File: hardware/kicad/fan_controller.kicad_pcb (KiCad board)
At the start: 2 copper layers, 75 x 60 mm, 84 parts, among them J1 12V IN, J10 AIN2, J11 AIN3, J12 AIN4, J13 AIN5, J14 AIN6, J2 BluePill A, J3 BluePill B, J4 USB int, J5 FAN1, J6 FAN2, J7 FAN3, J8 FAN4, J9 AIN1, Q1 BSS138, Q2 BSS138, Q3 BSS138, Q4 BSS138, U1 USBLC6-2SC6

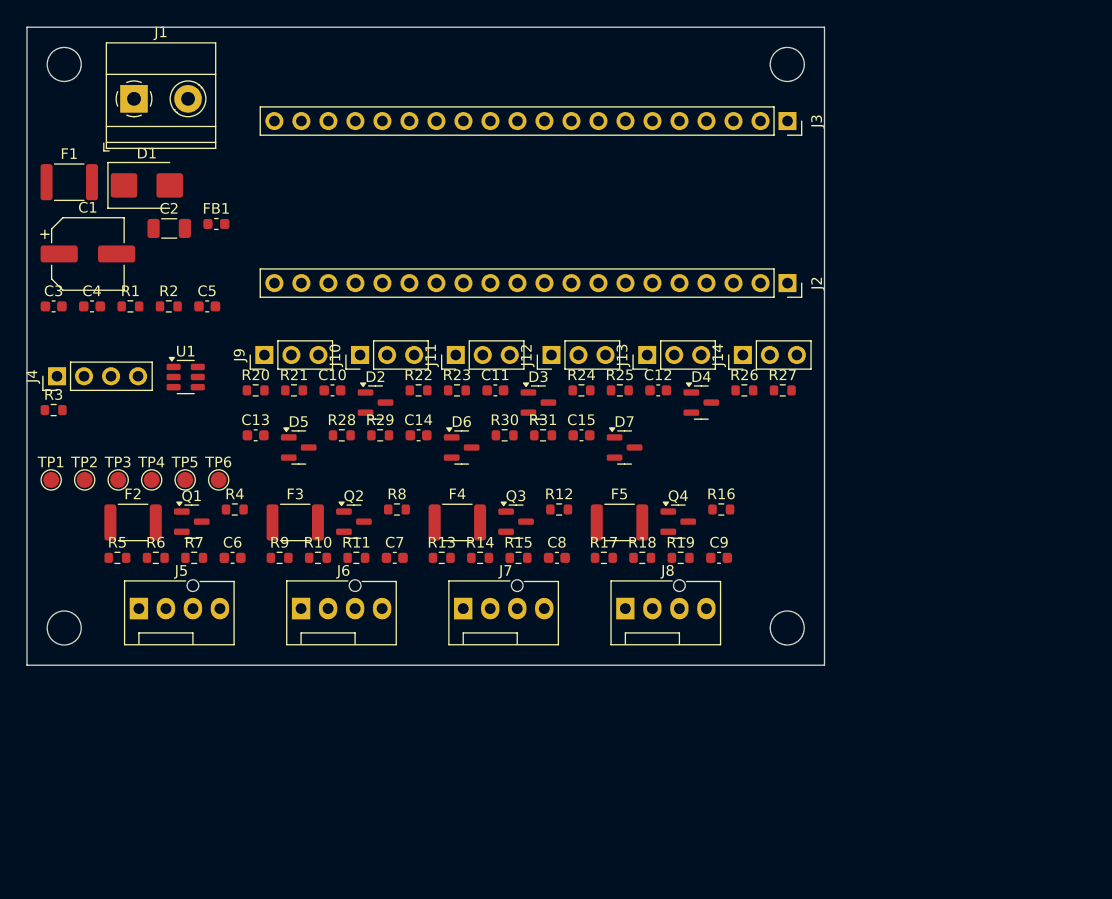
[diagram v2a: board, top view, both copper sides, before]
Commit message: hw: resave project in KiCad 10 file format
Signed-off-by: Roman Skakun <rm.skakun@gmail.com>
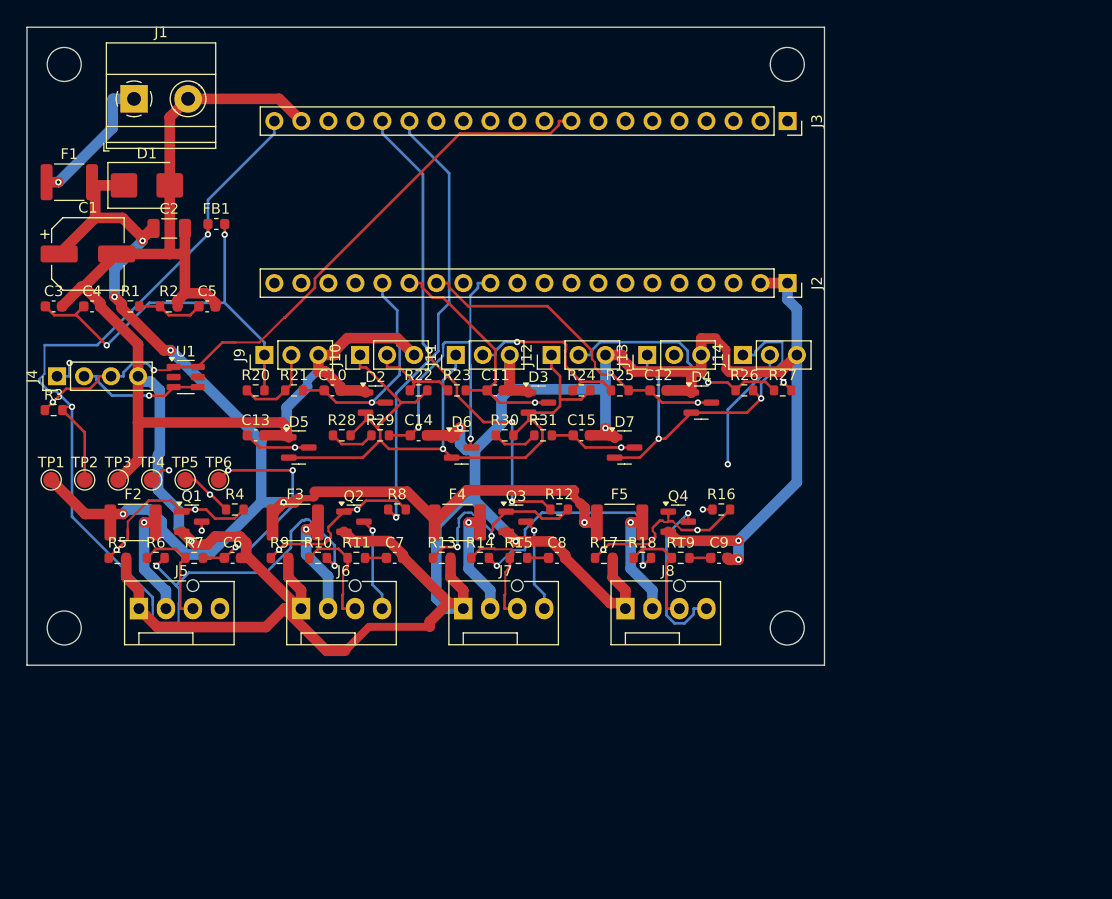
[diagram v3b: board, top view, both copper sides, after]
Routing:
- net GND: track 0.00 -> 370.6 mm, vias 0 -> 7
- net +3V3A: track 0.00 -> 144.6 mm, vias 0 -> 5
- net +3V3: track 0.00 -> 129.1 mm, vias 0 -> 6
- net +12V: track 0.00 -> 115.5 mm, vias 0 -> 6
- net USB_DP: track 0.00 -> 62.5 mm, vias 0 -> 2
- net FAN3_PWM: track 0.00 -> 46.3 mm, vias 0 -> 3
- net FAN2_PWM: track 0.00 -> 41.9 mm, vias 0 -> 1
- net AIN3: track 0.00 -> 31.5 mm, vias 0 -> 1
- net AIN5: track 0.00 -> 31.5 mm, vias 0 -> 2
- net AIN2: track 0.00 -> 23.3 mm, vias 0 -> 1
- net AIN4_IN: track 0.00 -> 22.3 mm, vias 0 -> 1
- net AIN1: track 0.00 -> 21.2 mm, vias 0 -> 1
- net FAN1_TACH: track 0.00 -> 21.1 mm, vias 0 -> 3
- net FAN3_PWM_G: track 0.00 -> 19.3 mm, vias 0 -> 2
- net AIN3_IN: track 0.00 -> 17.1 mm, vias 0 -> 1
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
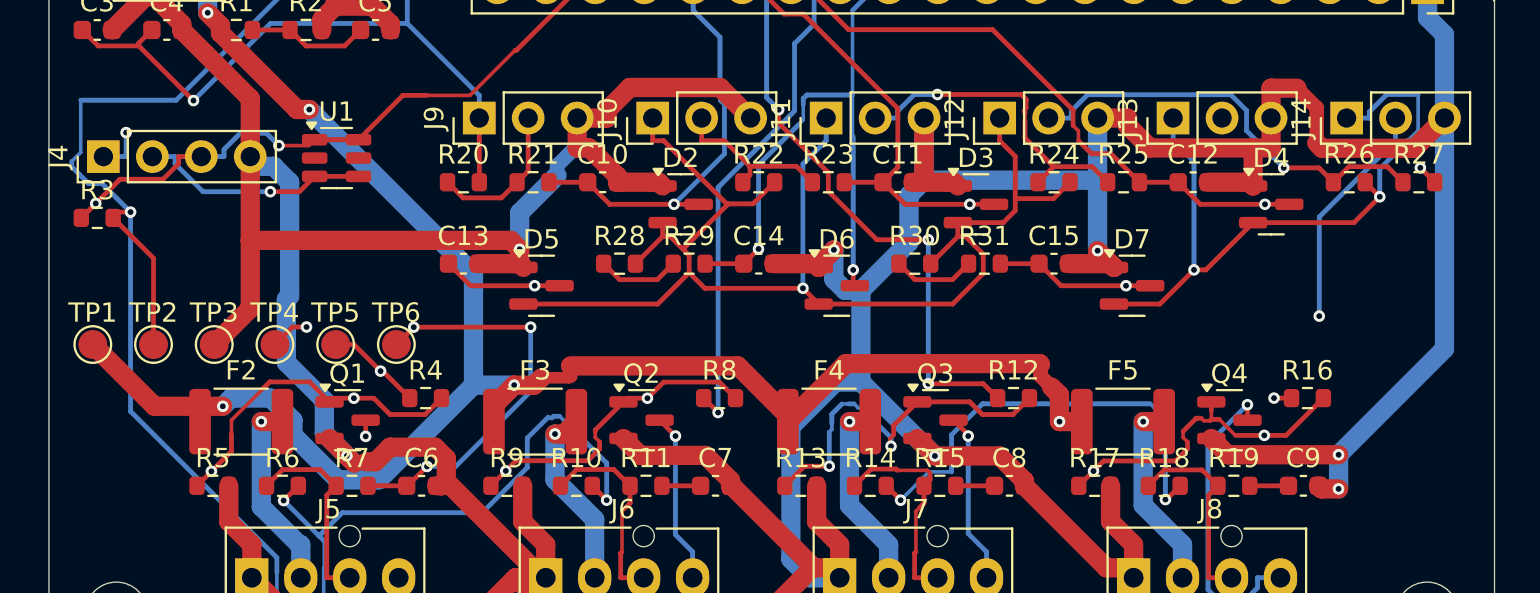
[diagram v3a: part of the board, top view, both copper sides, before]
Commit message: hw: remove dangling stub vias and traces from routing cleanup
20 vias left connected on only one copper layer, plus the short
track stubs feeding them, after an earlier routing edit. DRC now
reports 0 errors (was 0 before too) and 0 dangling-via/track
warnings; all affected nets remain fully connected.

Signed-off-by: Roman Skakun <rm.skakun@gmail.com>
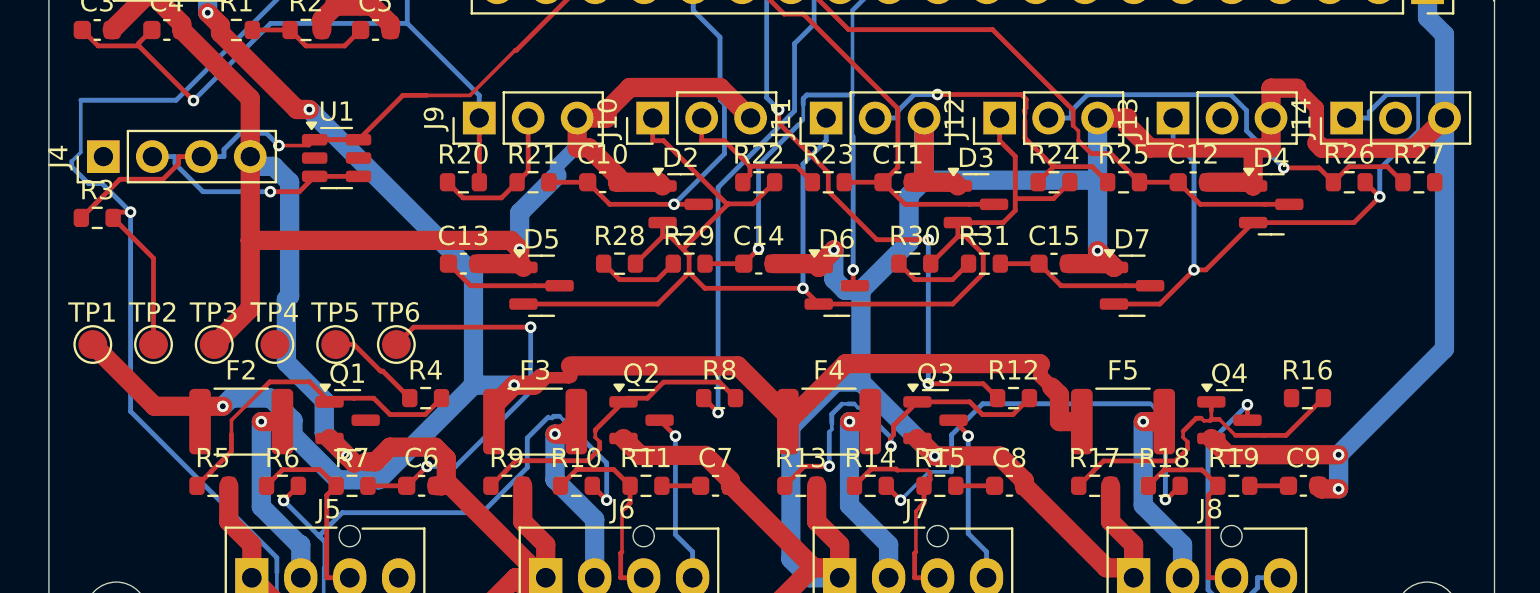
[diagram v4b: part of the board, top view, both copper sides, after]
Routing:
- net AIN6_IN: track 16.2 -> 4.30 mm, vias 1 -> 0
- net +5V: track 2.42 -> 0.00 mm, vias 1 -> 0
- net NRST: track 2.02 -> 0.00 mm, vias 1 -> 0
- net AIN4: track 7.29 -> 6.24 mm, vias 2 -> 0
- net FAN4_PWM: track 0.91 -> 0.00 mm, vias 1 -> 0
- net FAN1_PWM_OUT: track 0.84 -> 0.00 mm, vias 1 -> 0
- net USB_DP: vias 2 -> 1
- net FAN4_PWM_G: vias 2 -> 0
- net FAN2_PWM_G: vias 2 -> 0
- net FAN1_TACH: vias 3 -> 2
- net FAN1_PWM_G: vias 2 -> 0
- net FAN1_PWM: vias 1 -> 0
- net AIN6: vias 1 -> 0
- net AIN3: vias 1 -> 0
- net AIN2: vias 1 -> 0
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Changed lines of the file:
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@@
 		(net "FAN2_PWM_G")
 	)
-	(via
-		(at 23.7024 49.131)
-		(size 0.6)
-		(drill 0.3)
-		(layers "F.Cu" "B.Cu")
-		(net "FAN2_PWM_G")
-	)
-	(via
-		(at 31.0513 45.3609)
-		(size 0.6)
-		(drill 0.3)
-		(layers "F.Cu" "B.Cu")
-		(net "FAN2_PWM_G")
-	)
 	(segment
 		(start 33.865 30.825)
@@
 		(net "AIN2")
 	)
-	(via
-		(at 47.7772 35.3)
-		(size 0.6)
-		(drill 0.3)
-		(layers "F.Cu" "B.Cu")
-		(net "AIN2")
-	)
 	(segment
 		(start 64.31 49.905)
@@
 		(net "FAN1_PWM_G")
 	)
-	(via
-		(at 8.4289 49.1545)
-		(size 0.6)
-		(drill 0.3)
-		(layers "F.Cu" "B.Cu")
-		(net "FAN1_PWM_G")
-	)
-	(via
-		(at 15.8212 45.3609)
-		(size 0.6)
-		(drill 0.3)
-		(layers "F.Cu" "B.Cu")
-		(net "FAN1_PWM_G")
-	)
-	(segment
-		(start 71.9 34.155)
-		(end 71.1523 33.4073)
-		(width 0.25)
-		(layer "F.Cu")
-		(net "AIN4")
-	)
 	(segment
 		(start 21.875 39.525)
@@
 		(net "AIN4")
 	)
-	(via
-		(at 71.1523 33.4073)
-		(size 0.6)
-		(drill 0.3)
-		(layers "F.Cu" "B.Cu")
-		(net "AIN4")
-	)
-	(via
-		(at 25.2016 39.525)
-		(size 0.6)
-		(drill 0.3)
-		(layers "F.Cu" "B.Cu")
-		(net "AIN4")
-	)
-	(segment
-		(start 63.5596 45.355)
-		(end 64.47 45.355)
-		(width 0.25)
-		(layer "F.Cu")
-		(net "FAN4_PWM")
-	)
-	(via
-		(at 63.5596 45.355)
-		(size 0.6)
-		(drill 0.3)
-		(layers "F.Cu" "B.Cu")
-		(net "FAN4_PWM")
-	)
 	(segment
 		(start 61.5573 47.2894)
@@
 		(net "FAN4_PWM_G")
 	)
-	(via
-		(at 54.1955 49.1395)
-		(size 0.6)
-		(drill 0.3)
-		(layers "F.Cu" "B.Cu")
-		(net "FAN4_PWM_G")
-	)
-	(via
-		(at 63.0561 47.2894)
-		(size 0.6)
-		(drill 0.3)
-		(layers "F.Cu" "B.Cu")
-		(net "FAN4_PWM_G")
-	)
 	(segment
 		(start 36.05 38.38)
@@
 	)
 	(via
-		(at 52.4304 46.575)
-		(size 0.6)
-		(drill 0.3)
-		(layers "F.Cu" "B.Cu")
-		(net "+12V")
-	)
-	(via
 		(at 13.5105 30.3818)
 		(size 0.6)
@@
 		(net "USB_DP")
 	)
-	(via
-		(at 2.4287 35.2563)
-		(size 0.6)
-		(drill 0.3)
-		(layers "F.Cu" "B.Cu")
-		(net "USB_DP")
-	)
 	(segment
 		(start 9.0817 32.4573)
@@
 	)
 	(via
-		(at 18.9257 41.6743)
-		(size 0.6)
-		(drill 0.3)
-		(layers "F.Cu" "B.Cu")
-		(net "FAN1_TACH")
-	)
-	(via
 		(at 24.9919 41.6743)
 		(size 0.6)
@@
 		(net "AIN6")
 	)
-	(via
-		(at 55.8817 39.525)
-		(size 0.6)
-		(drill 0.3)
-		(layers "F.Cu" "B.Cu")
-		(net "AIN6")
-	)
 	(segment
 		(start 40.435 33.6579)
@@
 	)
 	(segment
-		(start 12.6337 41.6663)
-		(end 13.3644 41.6663)
-		(width 0.25)
-		(layer "F.Cu")
-		(net "NRST")
-	)
-	(segment
-		(start 11.725 42.575)
-		(end 12.6337 41.6663)
-		(width 0.25)
-		(layer "F.Cu")
-		(net "NRST")
-	)
-	(via
-		(at 13.3644 41.6663)
-		(size 0.6)
-		(drill 0.3)
-		(layers "F.Cu" "B.Cu")
-		(net "NRST")
-	)
-	(segment
 		(start 15.3411 27.0839)
 		(end 16.17 26.255)
@@
 		(net "AIN3")
 	)
-	(via
-		(at 63.0906 35.3)
-		(size 0.6)
-		(drill 0.3)
-		(layers "F.Cu" "B.Cu")
-		(net "AIN3")
-	)
 	(segment
 		(start 27.95 34.155)
@@
 		(net "AIN6_IN")
 	)
-	(via
-		(at 65.9073 41.1008)
-		(size 0.6)
-		(drill 0.3)
-		(layers "F.Cu" "B.Cu")
-		(net "AIN6_IN")
-	)
-	(segment
-		(start 65.9073 35.9594)
-		(end 65.9073 41.1008)
-		(width 0.25)
-		(layer "B.Cu")
-		(net "AIN6_IN")
-	)
-	(segment
-		(start 69.865 30.825)
-		(end 69.865 32.0017)
-		(width 0.25)
-		(layer "B.Cu")
-		(net "AIN6_IN")
-	)
-	(segment
-		(start 69.865 32.0017)
-		(end 65.9073 35.9594)
-		(width 0.25)
-		(layer "B.Cu")
-		(net "AIN6_IN")
-	)
 	(segment
 		(start 47.6946 47.2621)
@@
 	)
 	(segment
-		(start 16.4325 47.3412)
-		(end 16.4325 46.5)
-		(width 0.25)
-		(layer "F.Cu")
-		(net "FAN1_PWM_OUT")
-	)
-	(via
-		(at 16.4325 47.3412)
-		(size 0.6)
-		(drill 0.3)
-		(layers "F.Cu" "B.Cu")
-		(net "FAN1_PWM_OUT")
-	)
-	(segment
 		(start 17.3189 43.9539)
 		(end 18.72 45.355)
@@
 		(net "FAN1_PWM")
 	)
-	(via
-		(at 17.2048 43.9539)
-		(size 0.6)
-		(drill 0.3)
-		(layers "F.Cu" "B.Cu")
-		(net "FAN1_PWM")
-	)
 	(segment
 		(start 50.637 31.8566)
@@
 		(net "USB_DM")
 	)
-	(via
-		(at 4.0017 31.5797)
-		(size 0.6)
-		(drill 0.3)
-		(layers "F.Cu" "B.Cu")
-		(net "+5V")
-	)
-	(segment
-		(start 4.0017 32.825)
-		(end 4.0017 31.5797)
-		(width 0.25)
-		(layer "B.Cu")
-		(net "+5V")
-	)
-	(segment
-		(start 2.825 32.825)
-		(end 4.0017 32.825)
-		(width 0.25)
-		(layer "B.Cu")
-		(net "+5V")
-	)
 	(segment

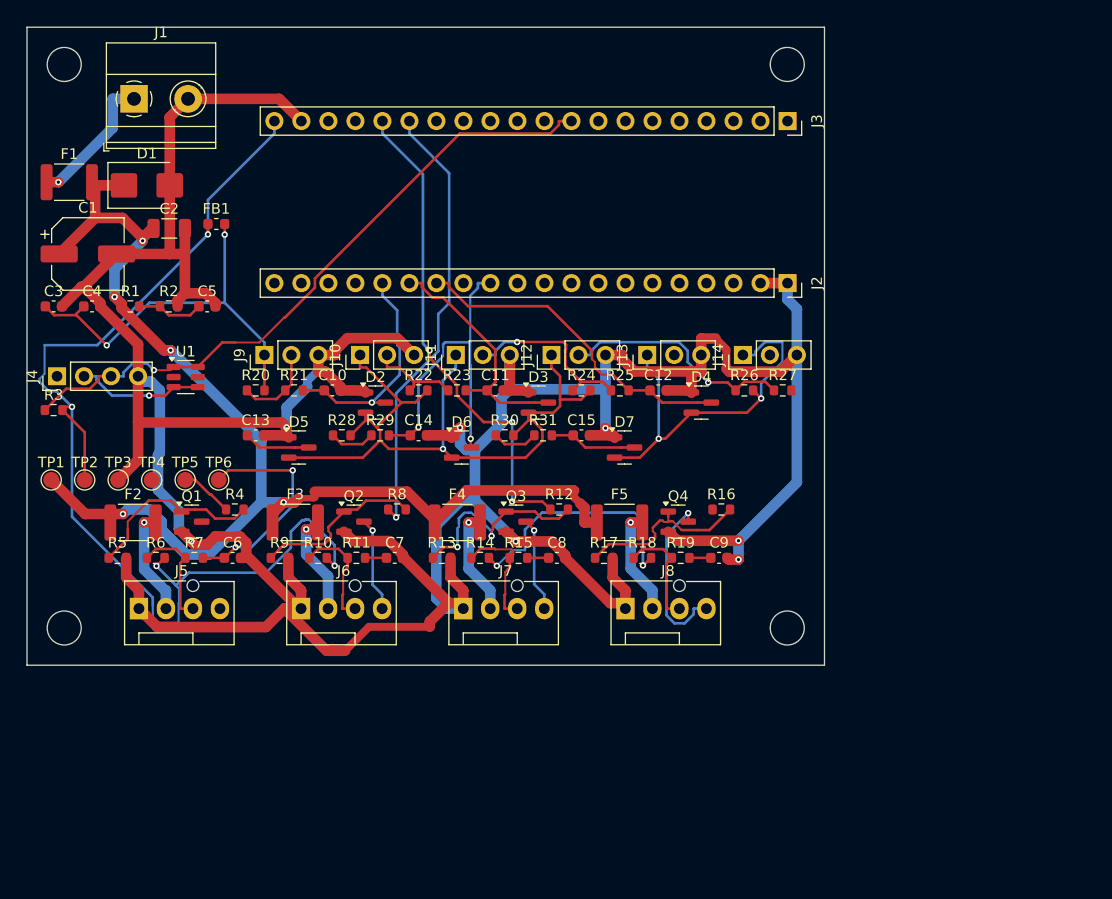
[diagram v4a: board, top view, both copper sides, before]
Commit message: hw: route 21 missing nets, remove 3V3/GND test point pair
21 nets (mostly BluePill header J2/J3 to main-board parts) were
never actually routed, despite earlier DRC checks reporting zero
errors - the MCP DRC wrapper used doesn't run KiCad's unconnected-
items check. Verified with native kicad-cli --severity-all.

Routed via Freerouting (autoroute, best-of-3), then manually closed
the 2 nets it couldn't finish (GND, +3V3A) and fixed a short the
autorouted +3V3A trace made against an existing GND track, plus a
board-edge clearance violation on FAN3_TACH.

Also removed TP2 (+3V3) / TP3 (GND), a probe pair that served no
circuit function, plus their stub traces.

Native kicad-cli DRC (10.0.7): 0 errors, 0 unconnected items.

Signed-off-by: Roman Skakun <rm.skakun@gmail.com>
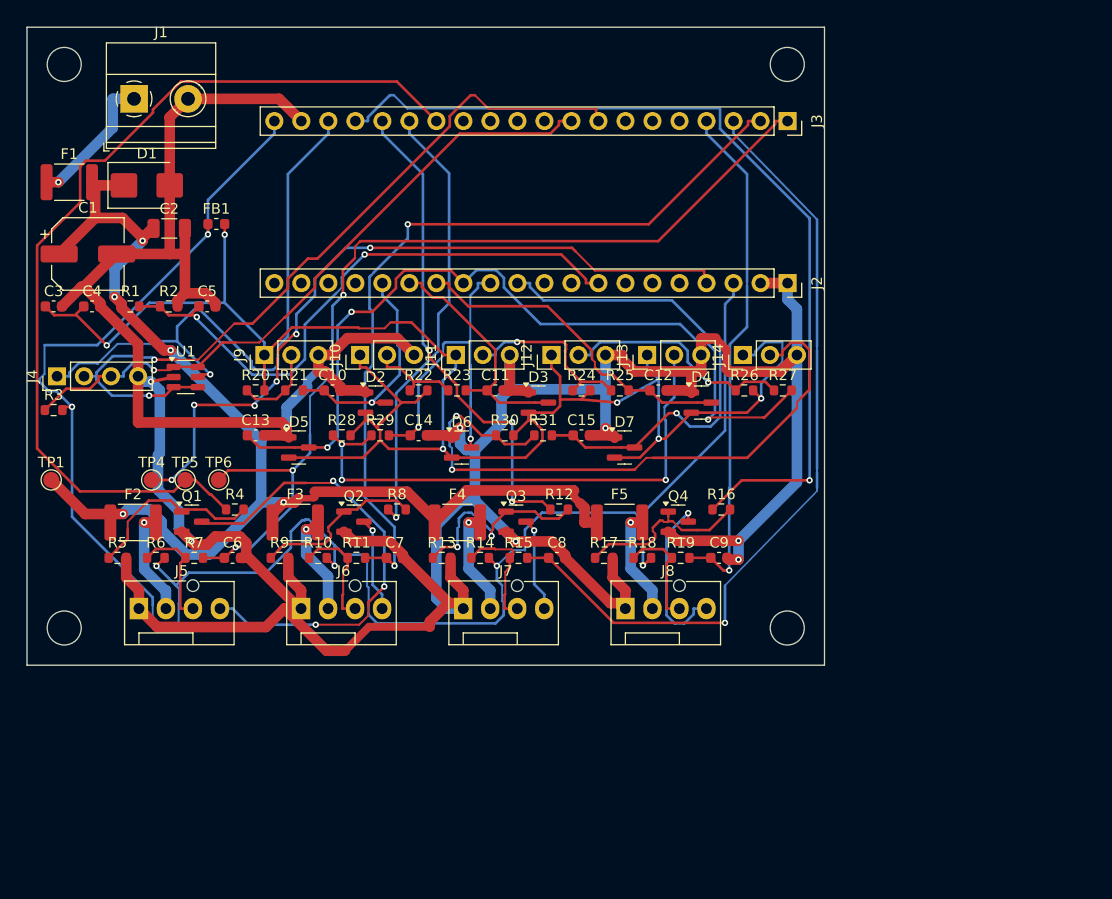
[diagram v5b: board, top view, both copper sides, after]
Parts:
- removed TP2: +3V3, TestPoint:TestPoint_Pad_D1.5mm
- removed TP3: GND, TestPoint:TestPoint_Pad_D1.5mm
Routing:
- net FAN4_PWM: track 0.00 -> 84.7 mm, vias 0 -> 1
- net FAN1_PWM: track 5.00 -> 87.8 mm
- net FAN2_TACH: track 2.01 -> 75.7 mm, vias 0 -> 2
- net FAN3_TACH: track 2.01 -> 75.0 mm, vias 0 -> 1
- net AIN4: track 6.24 -> 78.4 mm, vias 0 -> 3
- net NRST: track 0.00 -> 69.9 mm, vias 0 -> 6
- net FAN1_TACH: track 21.1 -> 90.4 mm, vias 2 -> 3
- net USB_DM: track 12.0 -> 73.3 mm, vias 1 -> 2
- net +5V: track 0.00 -> 57.9 mm, vias 0 -> 1
- net AIN6_IN: track 4.30 -> 59.7 mm, vias 0 -> 2
- net V12_SENSE: track 6.31 -> 55.6 mm, vias 0 -> 2
- net FAN4_TACH: track 2.01 -> 48.8 mm, vias 0 -> 1
- net AIN5_IN: track 4.30 -> 50.3 mm, vias 0 -> 3
- net +3V3: track 129.1 -> 174.8 mm
- net FAN1_PWM_OUT: track 0.00 -> 44.3 mm, vias 0 -> 3
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
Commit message: hw: swap 12V connector to Mate-N-Lok, drop main-board USB, rotate J3
Replace J1 (2-pin Phoenix screw terminal) with TE Connectivity
350424-1, a 4-circuit Mate-N-Lok PCB header (2x GND + 2x VIN_12V,
12A/250V per pin, 0.2in pitch). Custom footprint built from the
part's real datasheet drawing (drill/pitch), registered as a
project-local fanctl.pretty library since no footprint libraries
are installed in this environment.

Remove the main-board USB path entirely (J4 header, U1 ESD chip,
R3 pullup): the Blue Pill module's own USB port covers this, so
routing USB_DP/USB_DM across the main board was unnecessary. This
also freed board area.

Rotate J3 (Blue Pill B header) 180 degrees in place, and relocate
the 12V input protection cluster (F1 fuse, D1 TVS, C1 bulk cap,
C2 10u cap, FB1 ferrite) into the space freed by the USB removal,
to fit the physically larger J1 connector without colliding with
J3's courtyard.

KNOWN INCOMPLETE: native kicad-cli --severity-all DRC currently
reports 5 unconnected items, 7 shorts, and 3 track crossings,
all localized to the relocated F1/D1/C1/C2/FB1 cluster and nearby
NRST routing. Needs one more Freerouting pass on +12V/GND/NRST/
+3V3A plus manual cleanup before this is fab-ready. gen_kicad.py
(the board's generator script / BOM source of truth) has not yet
been updated to match these changes.

Signed-off-by: Roman Skakun <rm.skakun@gmail.com>
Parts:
- removed J4: USB int, Connector_PinHeader_2.54mm:PinHeader_1x04_P2.54mm_Vertical
- removed R3: 1k8, Resistor_SMD:R_0603_1608Metric
- removed TP1: +12V, TestPoint:TestPoint_Pad_D1.5mm
- removed U1: USBLC6-2SC6, Package_TO_SOT_SMD:SOT-23-6
- J1: footprint TerminalBlock_Phoenix:TerminalBlock_Phoenix_MKDS-1,5-2-5.08_1x02_P5.08mm_Horizontal -> fanctl:ConnHeader_MateNLok_1x04_P5.08mm_Vertical
- moved FB1 20.0 mm to (16.5, 38.5)
- moved C1 16.5 mm to (9.00, 37.5)
- moved C2 16.4 mm to (16.5, 35.0)
- moved D1 16.4 mm to (15.0, 30.8)
- moved F1 14.9 mm to (4.00, 29.5)
- moved J1 13.3 mm to (11.1, 20.0), turned to 90 degrees
- moved Q3 0.08 mm to (45.9, 46.5)
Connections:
- J1 pad 2: GND -> VIN_12V
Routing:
- net USB_DM: track 73.3 -> 0.00 mm, vias 2 -> 0
- net USB_DP: track 62.5 -> 0.00 mm, vias 1 -> 0
- net +5V: track 57.9 -> 0.00 mm, vias 1 -> 0
- net +12V: track 115.5 -> 144.6 mm, vias 5 -> 6
- net FAN1_TACH: track 90.4 -> 107.6 mm, vias 3 -> 4
- net FAN1_PWM: track 87.8 -> 72.8 mm, vias 0 -> 1
- net +3V3: track 174.8 -> 189.1 mm, vias 6 -> 7
- net +3V3A: track 173.1 -> 160.1 mm, vias 6 -> 8
- net GND: track 366.6 -> 359.0 mm, vias 8 -> 6
- net FAN4_PWM: track 84.7 -> 78.4 mm, vias 1 -> 2
- net FAN3_PWM: track 46.3 -> 52.5 mm
- net VIN_12V: track 13.1 -> 18.4 mm
- net NRST: track 69.9 -> 73.5 mm, vias 6 -> 3
- net FAN3_PWM_G: track 19.3 -> 22.0 mm
- net FAN2_TACH: track 75.7 -> 73.1 mm
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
